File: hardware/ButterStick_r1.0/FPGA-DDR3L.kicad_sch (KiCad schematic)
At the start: 6 parts, among them U4 ECP5UM5G_85_CABGA381

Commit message: hw.r1d0: Review complete, gerbers generated
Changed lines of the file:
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@@
 (kicad_sch (version 20200618) (host eeschema "5.99.0-unknown-73168a9~101~ubuntu18.04.1")
-  (page 1 18)
+  (page 8 18)
   (paper "A4")
   (title_block
     (title "ButterStick")
-    (date "2020-07-16")
+    (date "2020-07-17")
     (rev "r1.0")
     (company "GsD")
@@
     (stroke (width 0.1524) (type solid) (color 0 0 0 0))
   )
-  (bus_entry (at 173.99 67.31) (size 2.54 2.54)
-    (stroke (width 0.1524) (type solid) (color 0 0 0 0))
-  )
   (bus_entry (at 173.99 72.39) (size 2.54 2.54)
     (stroke (width 0.1524) (type solid) (color 0 0 0 0))
@@
     (stroke (width 0.1524) (type solid) (color 0 0 0 0))
   )
-  (bus_entry (at 173.99 113.03) (size 2.54 2.54)
-    (stroke (width 0.1524) (type solid) (color 0 0 0 0))
-  )
   (bus_entry (at 173.99 115.57) (size 2.54 2.54)
     (stroke (width 0.1524) (type solid) (color 0 0 0 0))
@@
     (stroke (width 0.1524) (type solid) (color 0 0 0 0))
   )
+  (bus_entry (at 177.8 67.31) (size 2.54 2.54)
+    (stroke (width 0.1524) (type solid) (color 0 0 0 0))
+  )
+  (bus_entry (at 177.8 113.03) (size 2.54 2.54)
+    (stroke (width 0.1524) (type solid) (color 0 0 0 0))
+  )
   (wire (pts (xy 52.07 97.79) (xy 77.47 97.79))
     (stroke (width 0) (type solid) (color 0 0 0 0))
@@
     (stroke (width 0) (type solid) (color 0 0 0 0))
   )
-  (wire (pts (xy 176.53 67.31) (xy 200.66 67.31))
-    (stroke (width 0) (type solid) (color 0 0 0 0))
-  )
-  (wire (pts (xy 176.53 69.85) (xy 200.66 69.85))
+  (wire (pts (xy 176.53 66.04) (xy 179.07 66.04))
+    (stroke (width 0) (type solid) (color 0 0 0 0))
+  )
+  (wire (pts (xy 176.53 67.31) (xy 176.53 66.04))
     (stroke (width 0) (type solid) (color 0 0 0 0))
   )
@@
     (stroke (width 0) (type solid) (color 0 0 0 0))
   )
-  (wire (pts (xy 176.53 115.57) (xy 200.66 115.57))
-    (stroke (width 0) (type solid) (color 0 0 0 0))
-  )
   (wire (pts (xy 176.53 118.11) (xy 200.66 118.11))
     (stroke (width 0) (type solid) (color 0 0 0 0))
@@
     (stroke (width 0) (type solid) (color 0 0 0 0))
   )
+  (wire (pts (xy 179.07 66.04) (xy 179.07 67.31))
+    (stroke (width 0) (type solid) (color 0 0 0 0))
+  )
+  (wire (pts (xy 179.07 67.31) (xy 200.66 67.31))
+    (stroke (width 0) (type solid) (color 0 0 0 0))
+  )
   (wire (pts (xy 180.34 54.61) (xy 200.66 54.61))
     (stroke (width 0) (type solid) (color 0 0 0 0))
@@
     (stroke (width 0) (type solid) (color 0 0 0 0))
   )
+  (wire (pts (xy 180.34 69.85) (xy 200.66 69.85))
+    (stroke (width 0) (type solid) (color 0 0 0 0))
+  )
+  (wire (pts (xy 180.34 115.57) (xy 200.66 115.57))
+    (stroke (width 0) (type solid) (color 0 0 0 0))
+  )
   (wire (pts (xy 182.88 50.8) (xy 160.02 50.8))
     (stroke (width 0) (type solid) (color 0 0 0 0))
@@
     (stroke (width 0) (type solid) (color 0 0 0 0))
   )
-  (bus (pts (xy 80.01 54.61) (xy 80.01 57.15))
-    (stroke (width 0) (type solid) (color 0 0 0 0))
-  )
-  (bus (pts (xy 80.01 57.15) (xy 80.01 62.23))
-    (stroke (width 0) (type solid) (color 0 0 0 0))
-  )
-  (bus (pts (xy 80.01 62.23) (xy 80.01 67.31))
-    (stroke (width 0) (type solid) (color 0 0 0 0))
-  )
-  (bus (pts (xy 80.01 67.31) (xy 80.01 72.39))
-    (stroke (width 0) (type solid) (color 0 0 0 0))
-  )
-  (bus (pts (xy 80.01 72.39) (xy 80.01 77.47))
-    (stroke (width 0) (type solid) (color 0 0 0 0))
-  )
-  (bus (pts (xy 80.01 77.47) (xy 80.01 82.55))
-    (stroke (width 0) (type solid) (color 0 0 0 0))
-  )
-  (bus (pts (xy 80.01 82.55) (xy 80.01 85.09))
-    (stroke (width 0) (type solid) (color 0 0 0 0))
-  )
-  (bus (pts (xy 80.01 85.09) (xy 80.01 90.17))
-    (stroke (width 0) (type solid) (color 0 0 0 0))
-  )
-  (bus (pts (xy 80.01 90.17) (xy 80.01 100.33))
+  (bus (pts (xy 80.01 54.61) (xy 80.01 59.69))
+    (stroke (width 0) (type solid) (color 0 0 0 0))
+  )
+  (bus (pts (xy 80.01 59.69) (xy 80.01 64.77))
+    (stroke (width 0) (type solid) (color 0 0 0 0))
+  )
+  (bus (pts (xy 80.01 64.77) (xy 80.01 69.85))
+    (stroke (width 0) (type solid) (color 0 0 0 0))
+  )
+  (bus (pts (xy 80.01 69.85) (xy 80.01 74.93))
+    (stroke (width 0) (type solid) (color 0 0 0 0))
+  )
+  (bus (pts (xy 80.01 74.93) (xy 80.01 80.01))
+    (stroke (width 0) (type solid) (color 0 0 0 0))
+  )
+  (bus (pts (xy 80.01 80.01) (xy 80.01 85.09))
+    (stroke (width 0) (type solid) (color 0 0 0 0))
+  )
+  (bus (pts (xy 80.01 85.09) (xy 80.01 87.63))
+    (stroke (width 0) (type solid) (color 0 0 0 0))
+  )
+  (bus (pts (xy 80.01 87.63) (xy 80.01 97.79))
+    (stroke (width 0) (type solid) (color 0 0 0 0))
+  )
+  (bus (pts (xy 80.01 97.79) (xy 80.01 100.33))
     (stroke (width 0) (type solid) (color 0 0 0 0))
   )
@@
     (stroke (width 0) (type solid) (color 0 0 0 0))
   )
-  (bus (pts (xy 80.01 107.95) (xy 80.01 110.49))
-    (stroke (width 0) (type solid) (color 0 0 0 0))
-  )
-  (bus (pts (xy 80.01 110.49) (xy 80.01 115.57))
-    (stroke (width 0) (type solid) (color 0 0 0 0))
-  )
-  (bus (pts (xy 80.01 115.57) (xy 80.01 118.11))
+  (bus (pts (xy 80.01 107.95) (xy 80.01 113.03))
+    (stroke (width 0) (type solid) (color 0 0 0 0))
+  )
+  (bus (pts (xy 80.01 113.03) (xy 80.01 118.11))
     (stroke (width 0) (type solid) (color 0 0 0 0))
   )
@@
     (stroke (width 0) (type solid) (color 0 0 0 0))
   )
-  (bus (pts (xy 173.99 64.77) (xy 173.99 72.39))
-    (stroke (width 0) (type solid) (color 0 0 0 0))
-  )
-  (bus (pts (xy 173.99 72.39) (xy 173.99 77.47))
-    (stroke (width 0) (type solid) (color 0 0 0 0))
-  )
-  (bus (pts (xy 173.99 77.47) (xy 173.99 82.55))
+  (bus (pts (xy 173.99 64.77) (xy 173.99 74.93))
+    (stroke (width 0) (type solid) (color 0 0 0 0))
+  )
+  (bus (pts (xy 173.99 74.93) (xy 173.99 80.01))
+    (stroke (width 0) (type solid) (color 0 0 0 0))
+  )
+  (bus (pts (xy 173.99 80.01) (xy 173.99 82.55))
     (stroke (width 0) (type solid) (color 0 0 0 0))
   )
@@
     (stroke (width 0) (type solid) (color 0 0 0 0))
   )
-  (bus (pts (xy 173.99 105.41) (xy 173.99 113.03))
-    (stroke (width 0) (type solid) (color 0 0 0 0))
-  )
-  (bus (pts (xy 173.99 113.03) (xy 173.99 118.11))
-    (stroke (width 0) (type solid) (color 0 0 0 0))
-  )
-  (bus (pts (xy 173.99 118.11) (xy 173.99 123.19))
-    (stroke (width 0) (type solid) (color 0 0 0 0))
-  )
-  (bus (pts (xy 173.99 123.19) (xy 173.99 125.73))
+  (bus (pts (xy 173.99 105.41) (xy 173.99 115.57))
+    (stroke (width 0) (type solid) (color 0 0 0 0))
+  )
+  (bus (pts (xy 173.99 115.57) (xy 173.99 120.65))
+    (stroke (width 0) (type solid) (color 0 0 0 0))
+  )
+  (bus (pts (xy 173.99 120.65) (xy 173.99 125.73))
     (stroke (width 0) (type solid) (color 0 0 0 0))
   )
@@
     (stroke (width 0) (type solid) (color 0 0 0 0))
   )
+  (bus (pts (xy 177.8 54.61) (xy 177.8 113.03))
+    (stroke (width 0) (type solid) (color 0 0 0 0))
+  )

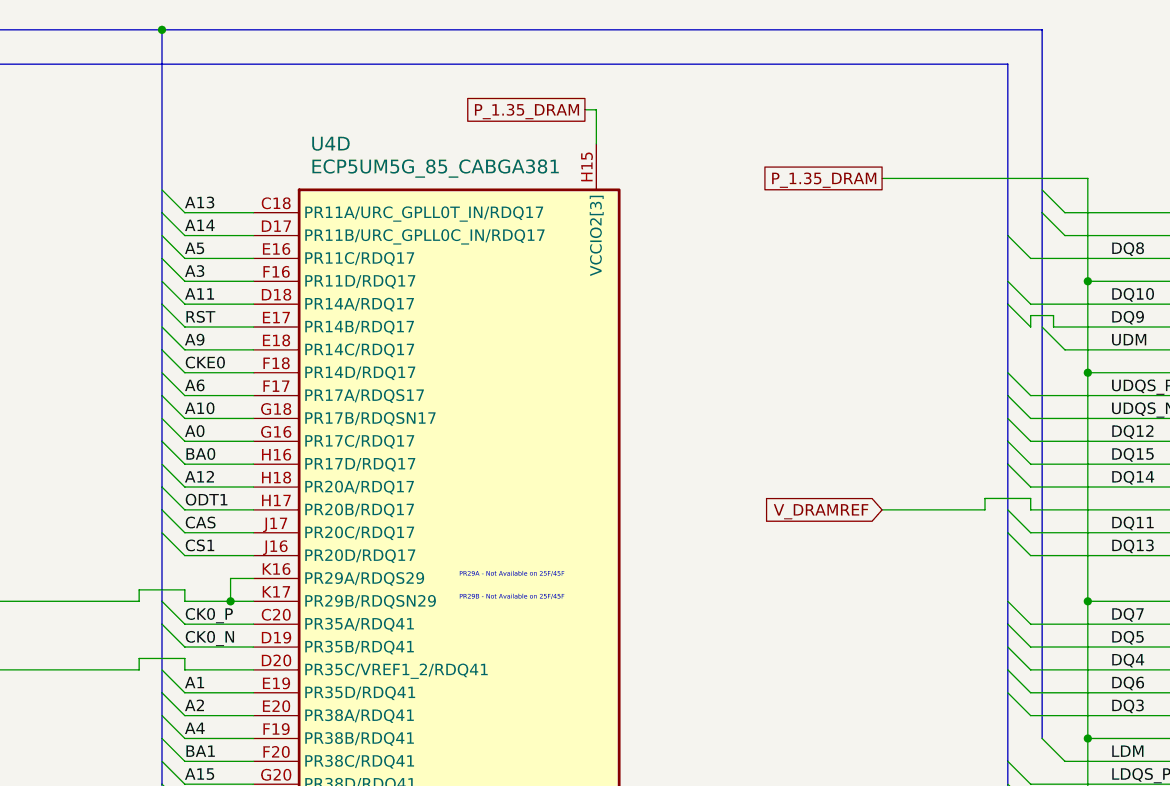
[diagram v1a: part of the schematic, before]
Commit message: hw.r1d0: Update BOM fieids in schematic.
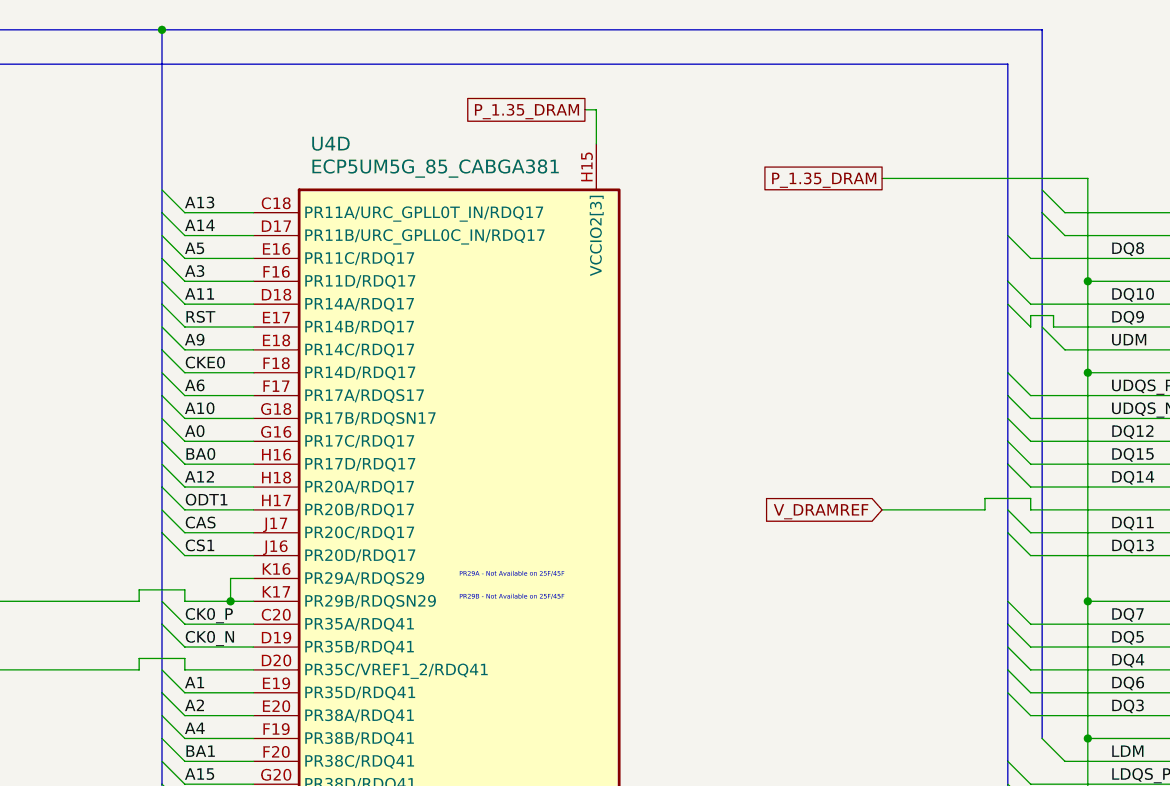
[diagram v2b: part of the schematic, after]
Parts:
- C33, C34, C35, C36, C37: Mfg (none) -> Yageo; PN (none) -> CC0402KRX5R6BB105
- U4: Mfg (none) -> Lattice Semiconductor Corporation; PN (none) -> LFE5UM5G-85F-8BG381C; manf# ECP5UM5G_85 -> (none)
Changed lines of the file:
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@@
 (kicad_sch (version 20200618) (host eeschema "5.99.0-unknown-73168a9~101~ubuntu18.04.1")
-  (page 8 18)
+  (page 1 18)
   (paper "A4")
   (title_block
@@
     (stroke (width 0) (type solid) (color 0 0 0 0))
   )
-  (bus (pts (xy 80.01 85.09) (xy 80.01 87.63))
-    (stroke (width 0) (type solid) (color 0 0 0 0))
-  )
-  (bus (pts (xy 80.01 87.63) (xy 80.01 97.79))
-    (stroke (width 0) (type solid) (color 0 0 0 0))
-  )
-  (bus (pts (xy 80.01 97.79) (xy 80.01 100.33))
+  (bus (pts (xy 80.01 85.09) (xy 80.01 90.17))
+    (stroke (width 0) (type solid) (color 0 0 0 0))
+  )
+  (bus (pts (xy 80.01 90.17) (xy 80.01 100.33))
     (stroke (width 0) (type solid) (color 0 0 0 0))
   )
@@
     (stroke (width 0) (type solid) (color 0 0 0 0))
   )
-  (bus (pts (xy 173.99 38.1) (xy 173.99 57.15))
-    (stroke (width 0) (type solid) (color 0 0 0 0))
-  )
-  (bus (pts (xy 173.99 57.15) (xy 173.99 64.77))
-    (stroke (width 0) (type solid) (color 0 0 0 0))
-  )
-  (bus (pts (xy 173.99 64.77) (xy 173.99 74.93))
+  (bus (pts (xy 173.99 38.1) (xy 173.99 62.23))
+    (stroke (width 0) (type solid) (color 0 0 0 0))
+  )
+  (bus (pts (xy 173.99 62.23) (xy 173.99 72.39))
+    (stroke (width 0) (type solid) (color 0 0 0 0))
+  )
+  (bus (pts (xy 173.99 72.39) (xy 173.99 74.93))
     (stroke (width 0) (type solid) (color 0 0 0 0))
   )
@@
       (effects (font (size 1.27 1.27)) hide)
     )
+    (property "Mfg" "Yageo" (id 4) (at 116.84 161.29 0)
+      (effects (font (size 1.27 1.27)) hide)
+    )
+    (property "PN" "CC0402KRX5R6BB105" (id 5) (at 116.84 161.29 0)
+      (effects (font (size 1.27 1.27)) hide)
+    )
   )
   (symbol (lib_id "Device:C") (at 127 161.29 0) (unit 1)
@@
       (effects (font (size 1.27 1.27)) hide)
     )
+    (property "Mfg" "Yageo" (id 4) (at 127 161.29 0)
+      (effects (font (size 1.27 1.27)) hide)
+    )
+    (property "PN" "CC0402KRX5R6BB105" (id 5) (at 127 161.29 0)
+      (effects (font (size 1.27 1.27)) hide)
+    )
   )
   (symbol (lib_id "Device:C") (at 137.16 161.29 0) (unit 1)
@@
       (effects (font (size 1.27 1.27)) hide)
     )
+    (property "Mfg" "Yageo" (id 4) (at 137.16 161.29 0)
+      (effects (font (size 1.27 1.27)) hide)
+    )
+    (property "PN" "CC0402KRX5R6BB105" (id 5) (at 137.16 161.29 0)
+      (effects (font (size 1.27 1.27)) hide)
+    )
   )
   (symbol (lib_id "Device:C") (at 147.32 161.29 0) (unit 1)
@@
       (effects (font (size 1.27 1.27)) hide)
     )
+    (property "Mfg" "Yageo" (id 4) (at 147.32 161.29 0)
+      (effects (font (size 1.27 1.27)) hide)
+    )
+    (property "PN" "CC0402KRX5R6BB105" (id 5) (at 147.32 161.29 0)
+      (effects (font (size 1.27 1.27)) hide)
+    )
   )
   (symbol (lib_id "Device:C") (at 157.48 161.29 0) (unit 1)
@@
       (effects (font (size 1.27 1.27)) hide)
     )
+    (property "Mfg" "Yageo" (id 4) (at 157.48 161.29 0)
+      (effects (font (size 1.27 1.27)) hide)
+    )
+    (property "PN" "CC0402KRX5R6BB105" (id 5) (at 157.48 161.29 0)
+      (effects (font (size 1.27 1.27)) hide)
+    )
   )
   (symbol (lib_id "gkl_lattice:ECP5UM5G_85_CABGA381") (at 200.66 54.61 0) (unit 5)
@@
       (effects (font (size 1.524 1.524)) (justify right) hide)
     )
-    (property "manf#" "ECP5UM5G_85" (id 4) (at 204.47 55.88 0)
+    (property "manf#" "" (id 4) (at 204.47 55.88 0)
       (effects (font (size 1.524 1.524)) (justify right) hide)
+    )
+    (property "Mfg" "Lattice Semiconductor Corporation" (id 4) (at 200.66 54.61 0)
+      (effects (font (size 1.27 1.27)) hide)
+    )
+    (property "PN" "LFE5UM5G-85F-8BG381C" (id 5) (at 200.66 54.61 0)
+      (effects (font (size 1.27 1.27)) hide)
     )
   )
@@
       (effects (font (size 1.524 1.524)) (justify right) hide)
     )
-    (property "manf#" "ECP5UM5G_85" (id 4) (at 93.98 55.88 0)
+    (property "manf#" "" (id 4) (at 93.98 55.88 0)
       (effects (font (size 1.524 1.524)) (justify right) hide)
     )
-  )
+    (property "Mfg" "Lattice Semiconductor Corporation" (id 4) (at 90.17 54.61 0)
+      (effects (font (size 1.27 1.27)) hide)
+    )
+    (property "PN" "LFE5UM5G-85F-8BG381C" (id 5) (at 90.17 54.61 0)
+      (effects (font (size 1.27 1.27)) hide)
+    )
+  )

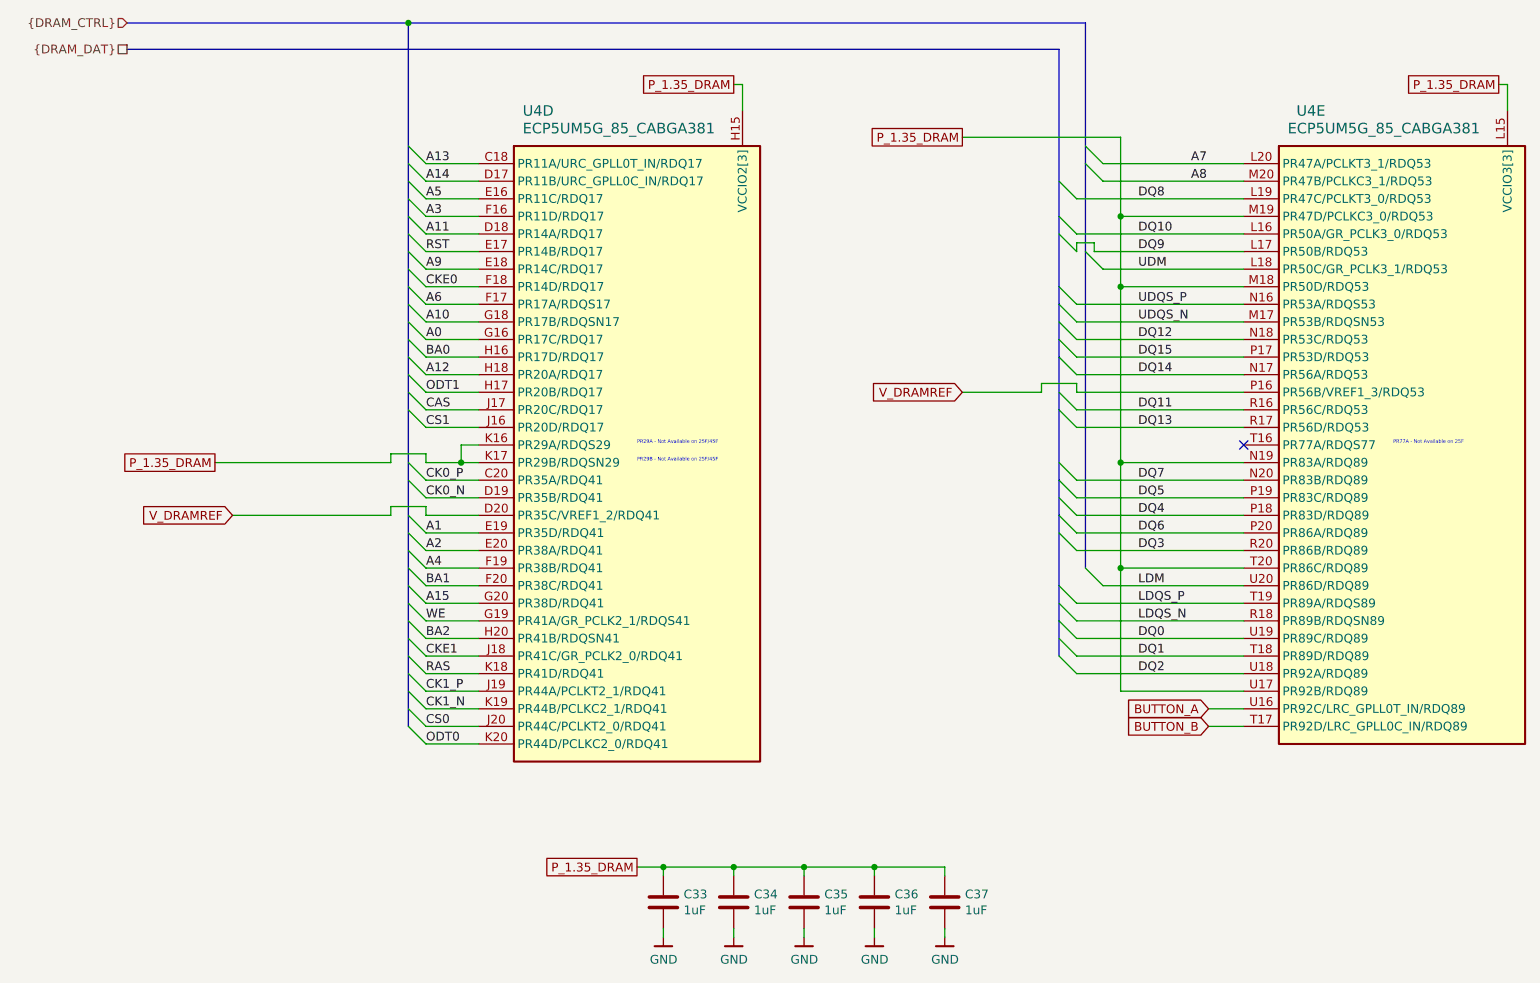
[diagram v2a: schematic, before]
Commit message: hw.r1d0: Fix RGMII straps
This commit correctly sets the stop resistos on the RGMII lines to 1K5
instead of DNP.
Also regenerate and add a schematic in PDF format.

Fixes #6
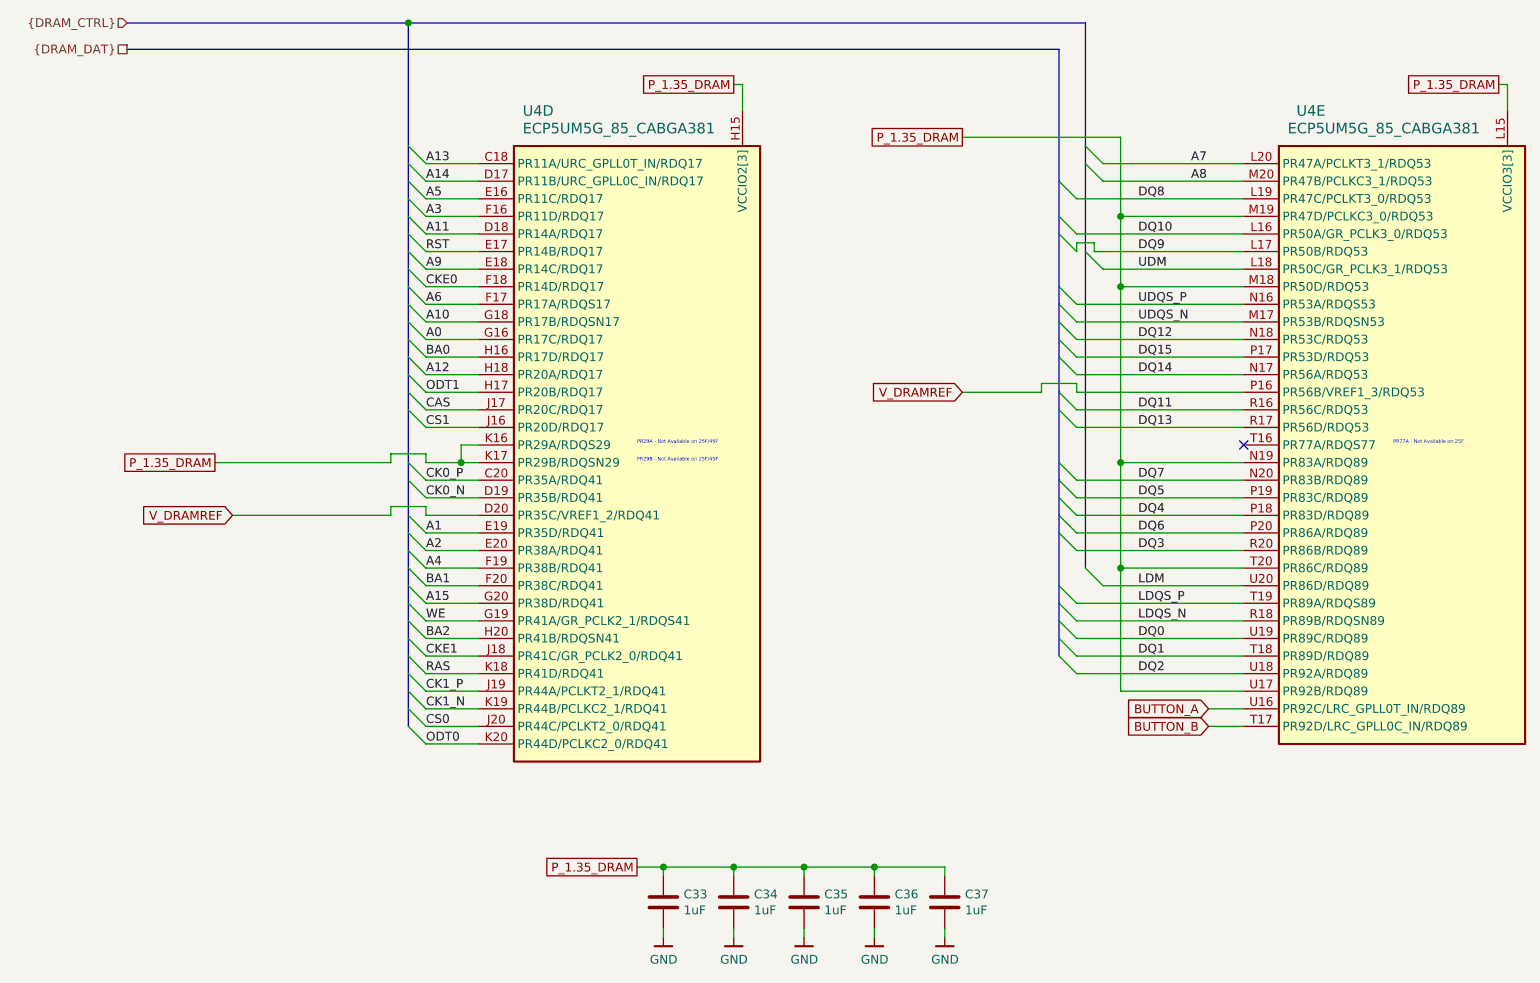
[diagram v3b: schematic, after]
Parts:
- U4: PN LFE5UM5G-85F-8BG381C -> LFE5UM5G-85F-8BG381I
